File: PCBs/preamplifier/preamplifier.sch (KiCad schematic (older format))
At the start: 63 parts, among them IC1 LTC6268, IC2 LTC6228, T1 CPH3910, X1 87437-0443

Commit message: Reorganization of pcb files
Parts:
- removed A1: SMA-EDGE-0.062, preamplifier:CONSMA003.062, symbol preamplifier-eagle-import:LINX-SMA-EDGE-0.062
- removed C17: 100n/50V, preamplifier:C0603, symbol preamplifier-eagle-import:C-EUC0603
- removed C18: 4,7u/6V, preamplifier:SMC_A, symbol preamplifier-eagle-import:CPOL-EUSMCA
- removed D10, D12, D14, D16, D18, D2, D20, D4, D6, D8: TEMD5010X01, preamplifier:DIODE_TEMD5010, symbol preamplifier-eagle-import:TEMD5010X01
- removed D11, D13, D15, D17, D19, D3, D5, D7, D9: VBPW34S, preamplifier:SOD6439X130N, symbol preamplifier-eagle-import:VBPW34S
- removed unit 2 of IC1
- removed IC2: LTC6228, preamplifier:TSOT23-6, symbol preamplifier-eagle-import:LTC6268
- removed LED1, LED2, LED3: GREEN, preamplifier:CHIPLED_0603, symbol preamplifier-eagle-import:LEDCHIPLED_0603
- removed R10, R11, R9: 1, preamplifier:R0603, symbol preamplifier-eagle-import:R-EU_R0603
- removed R3: 43k, preamplifier:R0603, symbol preamplifier-eagle-import:R-EU_R0603
- removed R4, R5: 300, preamplifier:R0603, symbol preamplifier-eagle-import:R-EU_R0603
- removed X1: 87437-0443, preamplifier:87437-0443, symbol preamplifier-eagle-import:87438-0487437-0443
- added C17: 100n/50V, Capacitor_SMD:C_0603_1608Metric, symbol Device:C
- added C18: 4,7u/6V, Capacitor_Tantalum_SMD:CP_EIA-3216-18_Kemet-A, symbol Device:CP
- added C19: 10p/50V, Capacitor_SMD:C_0603_1608Metric, symbol Device:C
- added D10, D2, D3, D4, D5, D6, D7, D8, D9: VBPW34S, semiconductor_radiation_detector:XDCR_VBPW34S, symbol semiconductor_radiation_detector:VBPW34S
- added J1: 874370443, semiconductor_radiation_detector:87437-0443, symbol semiconductor_radiation_detector:874370443
- added J2: CON-SMA-EDGE-S, semiconductor_radiation_detector:CON-SMA-EDGE-S, symbol semiconductor_radiation_detector:CON-SMA-EDGE-S
- added L1, L2, L3: 1u, Inductor_SMD:L_0603_1608Metric, symbol Device:L
- added RV1: 10, Potentiometer_SMD:Potentiometer_Bourns_3224W_Vertical, symbol Device:R_POT
- added unit 2 of U1
- added U2: LTC6228xS6, Package_TO_SOT_SMD:TSOT-23-6, symbol Amplifier_Operational:LTC6228xS6
- C1: value 4,7u/50V -> 4,7u/63V; footprint preamplifier:C1206 -> Capacitor_SMD:C_1206_3216Metric; symbol preamplifier-eagle-import:C-EUC1206 -> Device:C
- C10, C12, C13, C14, C2, C4, C6, C9: footprint preamplifier:C0603 -> Capacitor_SMD:C_0603_1608Metric; symbol preamplifier-eagle-import:C-EUC0603 -> Device:C
- C11, C15, C16, C8: footprint preamplifier:SMC_A -> Capacitor_Tantalum_SMD:CP_EIA-3216-18_Kemet-A; symbol preamplifier-eagle-import:CPOL-EUSMCA -> Device:CP
- C3: footprint preamplifier:C1206 -> Capacitor_SMD:C_1206_3216Metric; symbol preamplifier-eagle-import:C-EUC1206 -> Device:C
- C5, C7: footprint preamplifier:SMC_B -> Capacitor_Tantalum_SMD:CP_EIA-3528-21_Kemet-B; symbol preamplifier-eagle-import:CPOL-EUSMCB -> Device:CP
- D1: footprint preamplifier:SOD6439X130N -> semiconductor_radiation_detector:XDCR_VBPW34S; symbol preamplifier-eagle-import:VBPW34S -> semiconductor_radiation_detector:VBPW34S; MANUFACTURER (none) -> Vishay; MAXIMUM_PACKAGE_HEIGHT (none) -> 1.4mm; PARTREV (none) -> 1.2; STANDARD (none) -> Manufacturer Recommendations
- R1, R12, R14, R15, R16, R17, R2, R6, R7, R8: footprint preamplifier:R0603 -> Resistor_SMD:R_0603_1608Metric; symbol preamplifier-eagle-import:R-EU_R0603 -> Device:R
- R13: value 92 -> 100; footprint preamplifier:R0603 -> Resistor_SMD:R_0603_1608Metric; symbol preamplifier-eagle-import:R-EU_R0603 -> Device:R
- T1: footprint preamplifier:SOT23 -> Package_TO_SOT_SMD:SOT-23; symbol preamplifier-eagle-import:CPH3910 -> Device:Q_NJFET_SDG
- U1: renamed from IC1; footprint preamplifier:TSOT23-6 -> Package_TO_SOT_SMD:TSOT-23-6; symbol preamplifier-eagle-import:LTC6268 -> semiconductor_radiation_detector:LTC6268
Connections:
- net +5V: now also C5.1, R12.1, R6.1, J1.2_1 (2), J1.2_2 (2), L1.1, L2.1; no longer C5.+, R12.2, R6.2
- net +65V: now also J1.1_1 (1), J1.1_2 (1); no longer R2.1
- net -5V: now also C7.2, R1.2, J1.4_1 (4), J1.4_2 (4), L3.2; no longer C7.-, R1.1
- net GND: now also C11.2, C15.2, C16.1, C5.2, C7.1, C8.2, R13.2, R7.2, C17.2, C18.2, J1.3_1 (3), J1.3_2 (3), J2.2 (Ext), U1.2 (GND); no longer C11.-, C15.-, C16.+, C5.-, C7.+, C8.-, R13.1, R7.1
- net LOC+5V: now also C11.1, L1.2, U1.6 (VDD); no longer C11.+
- net at C1.2, T1.2 (D): now also R1.1; no longer R1.2
- net at C12.2, D1.A, T1.3 (G)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: now also R8.1, D10.A, D2.A, D3.A, D4.A, D5.A, D6.A, D7.A, D8.A, D9.A; no longer R8.2
- net at R14.2: now also C17.1, C18.1, RV1.2; no longer R17.1
- net LTC6268V-: now reaches C14.1
- net LTC6268V-: now also C16.2, L3.1, U2.2 (V-); no longer C16.-
- net at C12.1, U1.1 (OUT): now also R15.1, R8.2; no longer R15.2, R8.1
- net at R16.1: now also R15.2, U2.3 (+); no longer R15.1
- net at R17.2: now also R14.1, C19.1, U2.4 (-)
- net LTC6268V+: now reaches C13.2
- net LTC6268V+: now also C15.1, L2.2, U2.6 (V+); no longer C15.+
- new net: C19.2, J2.1 (In), R17.1, U2.1
- new net: R12.2, RV1.1
- new net: C1.1, D1.K, D10.K, D2.K, D3.K, D4.K, D5.K, D6.K, D7.K, D8.K, D9.K, R2.1
- new net: R13.1, RV1.3
- new net: C8.1, C9.2, R6.2, R7.1, U1.3 (+IN)
- new net +60V: R2.2
- no-connect marks 0 -> 2
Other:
- note added: "Power supply filtering\n"
- note added: "Transimpedance amplifier with DC substractor"
- note removed: "Local power supply filters"
- note removed: "Power supply connector"
- note removed: "R9-11 common \nresistors or ferrite \nbeads"
- note removed: "Transimpedance amplifier with substractor"

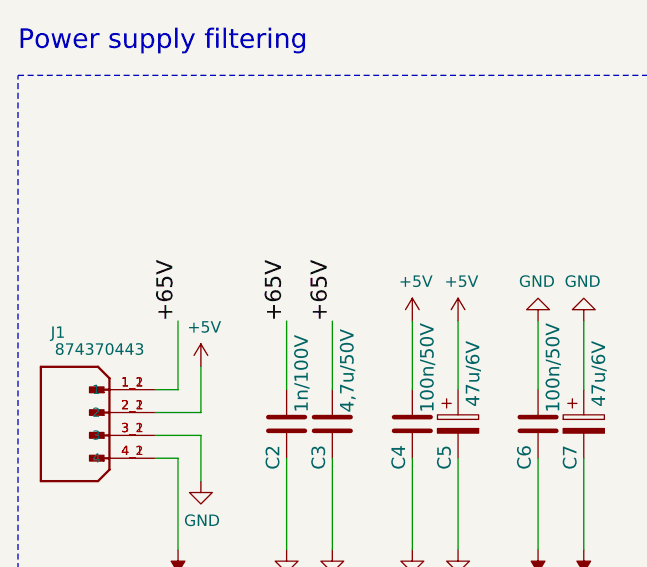
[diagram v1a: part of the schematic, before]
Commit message: finished preamplifier board redesigning
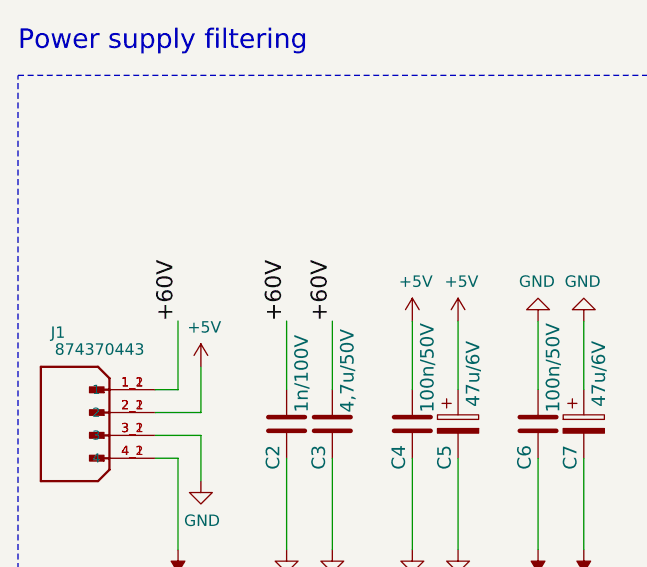
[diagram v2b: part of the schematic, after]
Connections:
- net +65V is gone; now on net +60V: C2.2, C3.1, J1.1_1 (1), J1.1_2 (1)
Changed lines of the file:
@@
 	2275 5375 2275 5675
 Text Label 2275 5375 1    70   ~ 0
-+65V
++60V
 Wire Wire Line
 	2475 5375 2475 5675
 Text Label 2475 5375 1    70   ~ 0
-+65V
++60V
 Wire Wire Line
 	1800 5675 1800 5375
@@
 	1700 5675 1800 5675
 Text Label 1800 5375 1    70   ~ 0
-+65V
++60V
 Text Label 1575 1950 2    70   ~ 0
 +60V
